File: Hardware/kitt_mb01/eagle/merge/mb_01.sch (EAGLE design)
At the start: 96 parts, among them CON1 ARDUINO_UNO, IC1.01 RT8293A, IC2.00 BQ24266RGET, IC3.01 LSM9DS1, P2 S2B-PH-K-S(LF)(SN), U6.01 TPS61032RSARPSDO-G16

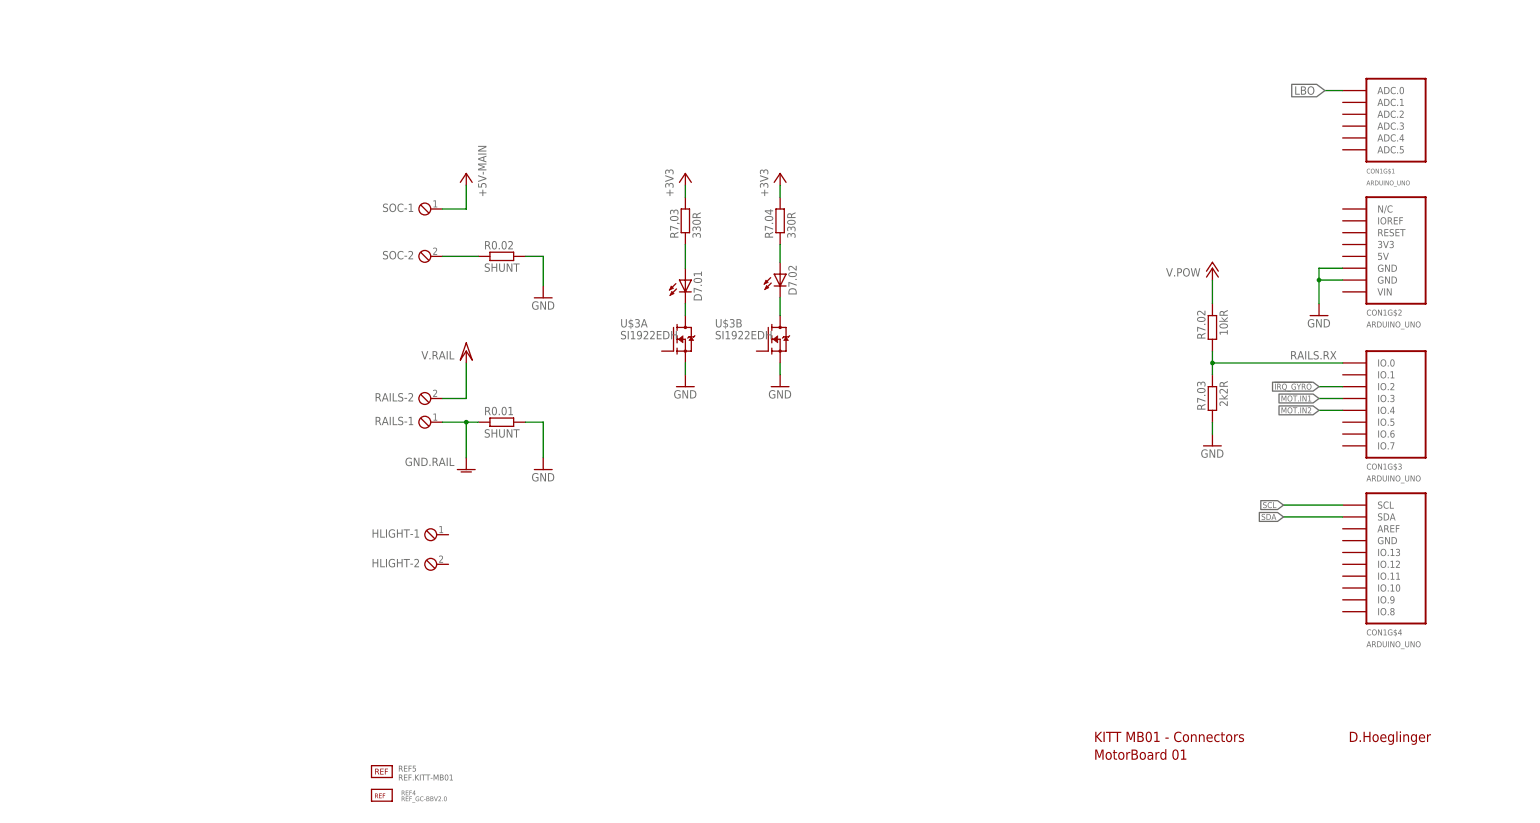
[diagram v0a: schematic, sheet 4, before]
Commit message: snapshot of board merge
a point about the flipped LEDs with a hole:
it's mounted in reverse with a hole as a makeshift lightguard,
...because maybe.
There are actual LEDs with an lens attached (see knightbright),
but regular ones work as well obviously.
Also it allows for text to be silk'd right next to it, which is sweet.
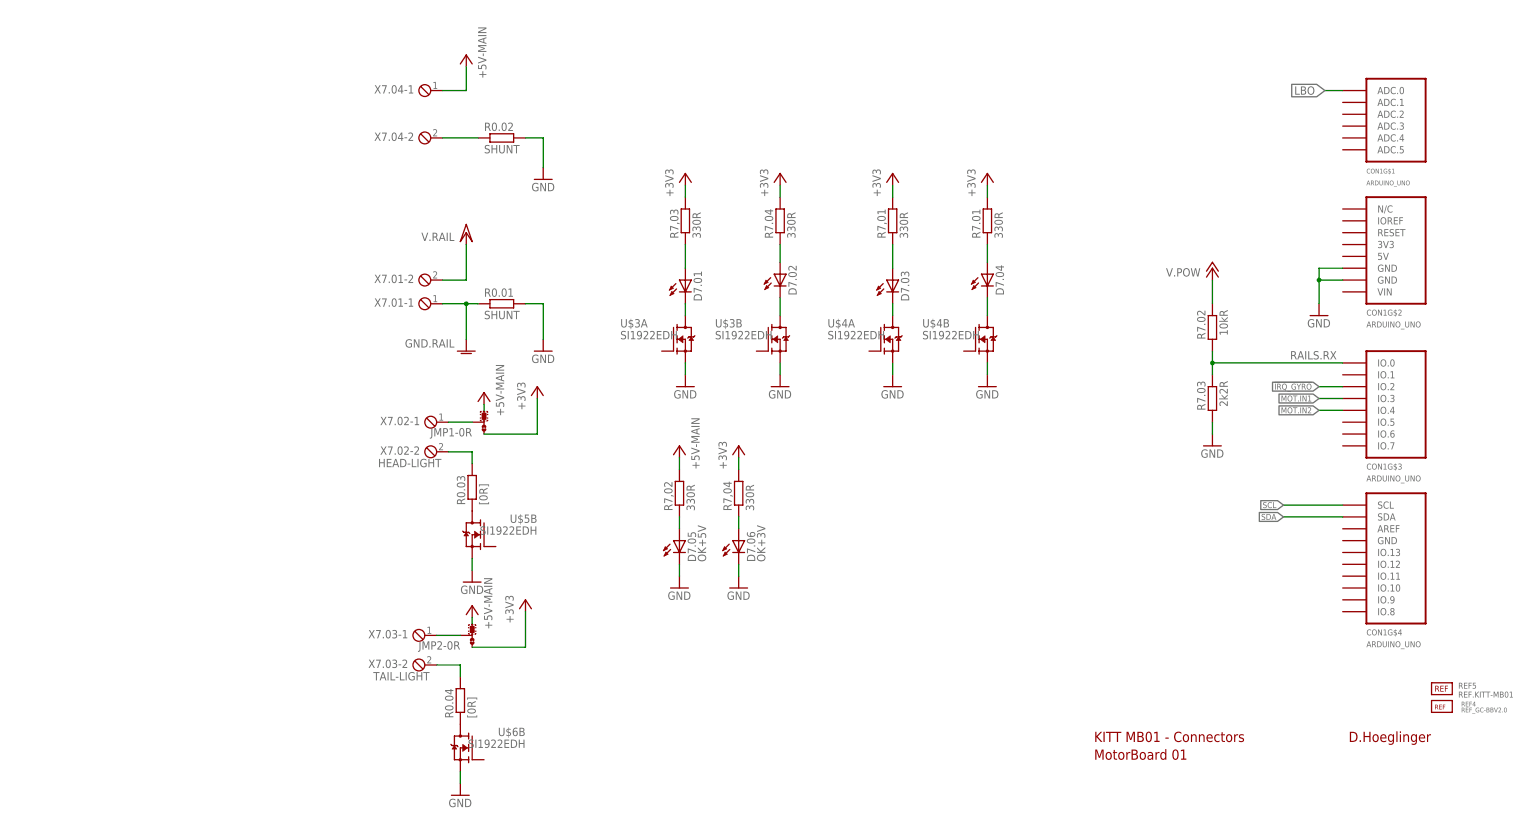
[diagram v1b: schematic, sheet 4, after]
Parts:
- removed HLIGHT, RAILS, SOC: (no value), con-phoenix-254:MPT2
- added D7.03, D7.04: (no value), led:LEDCHIPLED_0805
- added D7.05: OK+5V, led:LEDCHIPLED_1206
- added D7.06: OK+3V, led:LEDCHIPLED_1206
- added JMP1, JMP2: 0R-JUMPA, jump-0r-smd:0R-JUMPA
- added R0.03, R0.04: [0R], rcl:R-EU_R1206
- added R7,01, R7,02, R7,04, R7.01: 330R, rcl:R-EU_R0603
- added U$4, U$5, U$6: SI1922EDH, kitt.ic:SI1922EDH
- added X7.01, X7.04: (no value), con-phoenix-254:MPT2
- added X7.02: HEAD-LIGHT, con-phoenix-254:MPT2
- added X7.03: TAIL-LIGHT, con-phoenix-254:MPT2
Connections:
- new net N$28: D7.03.C, U$4A.D
- new net N$29: D7.03.A, R7,01.1
- new net N$30: D7.04.A, R7.01.1
- new net N$31: D7.04.C, U$4B.D
- new net N$32: D7.05.A, R7,02.1
- new net N$38: D7.06.A, R7,04.1
- new net N$42: R0.03.2, X7.02-2.1
- new net N$44: R0.03.1, U$5B.D
- new net N$45: JMP1-0R.2, X7.02-1.1
- new net N$46: R0.04.2, X7.03-2.1
- new net N$47: R0.04.1, U$6B.D
- new net N$48: JMP2-0R.2, X7.03-1.1
- net +3V3: now also JMP1-0R.1, JMP2-0R.1, R7,01.2, R7,04.2, R7.01.2
- net +5V: now also JMP1-0R.3, JMP2-0R.3, R7,02.2, X7.04-1.1; no longer SOC-1.1
- net GND: now also D7.05.C, D7.06.C, U$4A.S, U$4B.S, U$5B.S, U$6B.S
- net GNDA: now also X7.01-1.1; no longer RAILS-1.1
- net N$25: now also X7.04-2.1; no longer SOC-2.1
- net VCC/2: now also X7.01-2.1; no longer RAILS-2.1
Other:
- moved on the sheet: R0.01, R0.02, REF4, REF5

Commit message: snapshot of board merge - added possible port expander via i2c - did some more routing - connected battery indicator leds
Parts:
- added U1: MCP23017-E, kitt.ic:MCP23017-E
- D7.01, D7.02, D7.03, D7.04: device led:LEDCHIPLED_0805 -> led:LEDCHIPLED_1206
- X7.05: value (none) -> MOTOR
- renumbered SOC1 to X7.05
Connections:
- net IC2.0.!CHG: now also U$4A.G
- net IC2.0.!PG: now also U$4B.G
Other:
- note added: "TODO: INTERNAL PULLUP OR WHAT?"
- note added: "TODO: PORT EXPANDER? Pro: +Utility +Knight Rider Effects Con: -More $€ -More routes"

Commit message: snapshot of board merge  - it's going somewhere edition -
-> connected and routed head lights
-> did some power routing
-> next up: tail light
-> next² up: need for speedboards
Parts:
- removed U$5: SI1922EDH, kitt.ic:SI1922EDH
- added U7.01: SI1922EDH, kitt.ic:SI1922EDH
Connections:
- removed net N$44: R0.03.1, U$5B.D
- new net CAR.BLIGHT: CON1G$3.IO.5
- new net CAR.FLIGHT: CON1G$3.IO.6, U7.01A.G
- new net CAR.LAPCNT: CON1G$3.IO.7
- new net N$2: R0.03.1, U7.01A.D
- net GND: now also U7.01A.S; no longer U$5B.S
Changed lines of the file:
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@@
 <part name="+3V11" library="supply1" deviceset="+3V3" device=""/>
 <part name="P+5VMAIN4" library="supply1" deviceset="+5V" device="" value="+5V-MAIN"/>
-<part name="U$5" library="kitt.ic" deviceset="SI1922EDH" device=""/>
+<part name="U7.01" library="kitt.ic" deviceset="SI1922EDH" device=""/>
 <part name="R0.03" library="rcl" deviceset="R-EU_" device="R1206" value="[0R]"/>
 <part name="GND33" library="supply1" deviceset="GND" device=""/>
@@
 <instance part="+3V11" gate="G$1" x="86.36" y="83.82"/>
 <instance part="P+5VMAIN4" gate="1" x="73.66" y="83.82" rot="MR0"/>
-<instance part="U$5" gate="B" x="31.75" y="78.74" rot="MR0"/>
 <instance part="R0.03" gate="G$1" x="29.21" y="88.9" rot="R90"/>
 <instance part="GND33" gate="1" x="29.21" y="68.58"/>
@@
 <instance part="P+5VMAIN6" gate="1" x="29.21" y="63.5" rot="MR0"/>
 <instance part="+3V12" gate="G$1" x="40.64" y="64.77"/>
+<instance part="U7.01" gate="A" x="31.75" y="78.74" rot="MR0"/>
 </instances>
 <busses>
@@
 <segment>
 <pinref part="GND33" gate="1" pin="GND"/>
-<pinref part="U$5" gate="B" pin="S"/>
 <wire x1="29.21" y1="71.12" x2="29.21" y2="73.66" width="0.1524" layer="91"/>
+<pinref part="U7.01" gate="A" pin="S"/>
 </segment>
 <segment>
@@
 </segment>
 </net>
-<net name="N$44" class="0">
-<segment>
-<pinref part="U$5" gate="B" pin="D"/>
-<pinref part="R0.03" gate="G$1" pin="1"/>
-</segment>
-</net>
 <net name="N$45" class="0">
 <segment>
@@
 </segment>
 </net>
+<net name="N$2" class="0">
+<segment>
+<pinref part="R0.03" gate="G$1" pin="1"/>
+<pinref part="U7.01" gate="A" pin="D"/>
+</segment>
+</net>
+<net name="CAR.FLIGHT" class="0">
+<segment>
+<pinref part="U7.01" gate="A" pin="G"/>
+<wire x1="34.29" y1="76.2" x2="43.18" y2="76.2" width="0.1524" layer="91"/>
+<label x="43.18" y="76.2" size="1.778" layer="95" xref="yes"/>
+</segment>
+<segment>
+<label x="210.82" y="86.36" size="1.27" layer="95" rot="R180" xref="yes"/>
+<pinref part="CON1" gate="G$3" pin="IO.6"/>
+<wire x1="210.82" y1="86.36" x2="215.9" y2="86.36" width="0.1524" layer="91"/>
+</segment>
+</net>
+<net name="CAR.BLIGHT" class="0">
+<segment>
+<label x="210.82" y="88.9" size="1.27" layer="95" rot="R180" xref="yes"/>
+<wire x1="210.82" y1="88.9" x2="215.9" y2="88.9" width="0.1524" layer="91"/>
+<pinref part="CON1" gate="G$3" pin="IO.5"/>
+</segment>
+</net>
+<net name="CAR.LAPCNT" class="0">
+<segment>
+<pinref part="CON1" gate="G$3" pin="IO.7"/>
+<wire x1="215.9" y1="83.82" x2="210.82" y2="83.82" width="0.1524" layer="91"/>
+<label x="210.82" y="83.82" size="1.27" layer="95" rot="R180" xref="yes"/>
+</segment>
+</net>

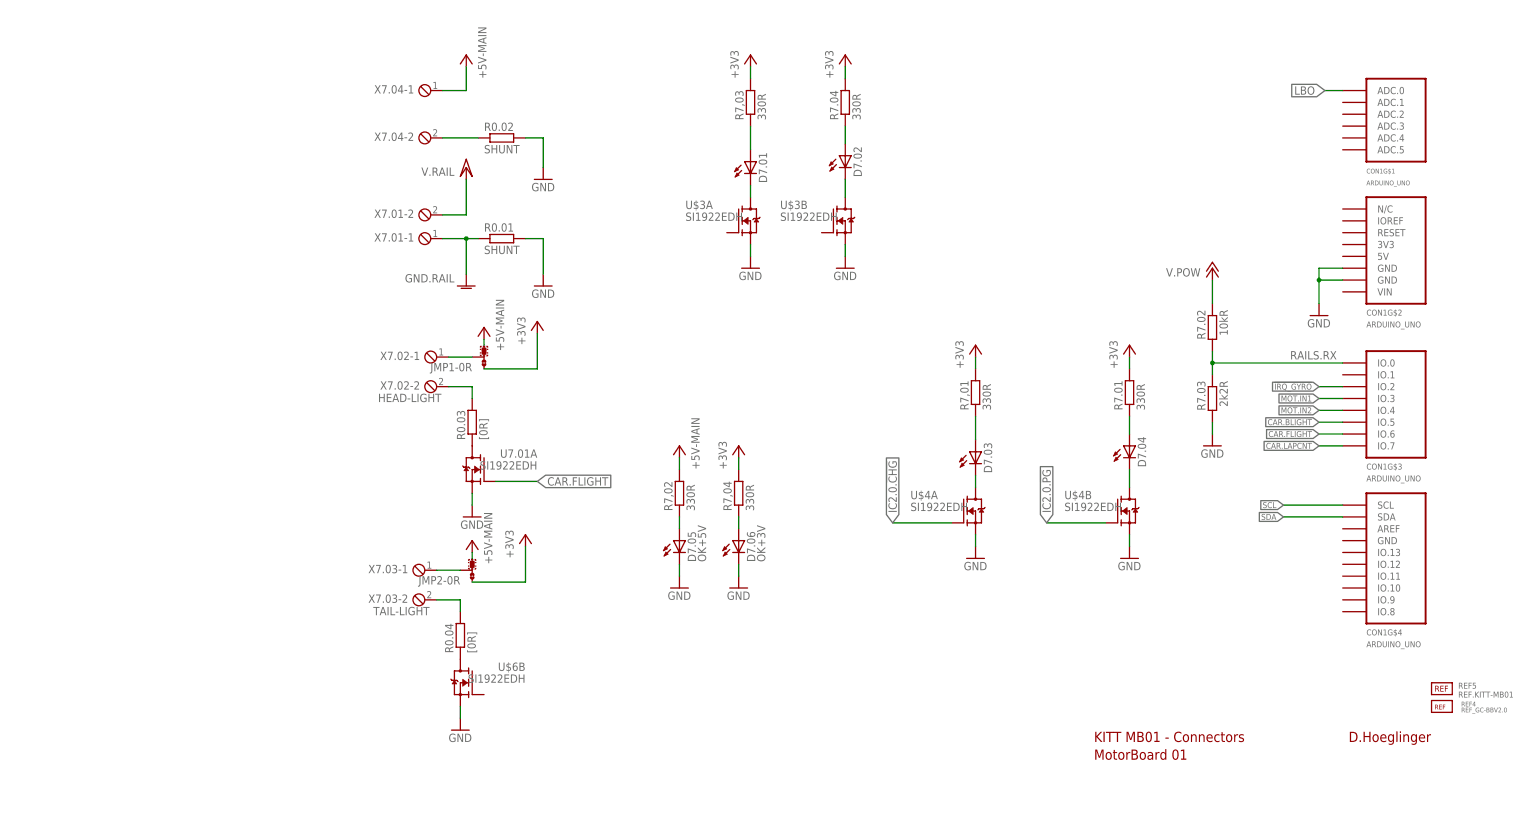
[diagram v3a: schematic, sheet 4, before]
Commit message: snapshot of board merge : nearing it's "completion" edition
things to do:
-> either find a good placement for GP-indicators,
   or drop alltogether (what purpose?)
-> (re)move idea about port expander (DB01 maybe?)
-> add some fancy-pants logos, fiducial marks and layer count
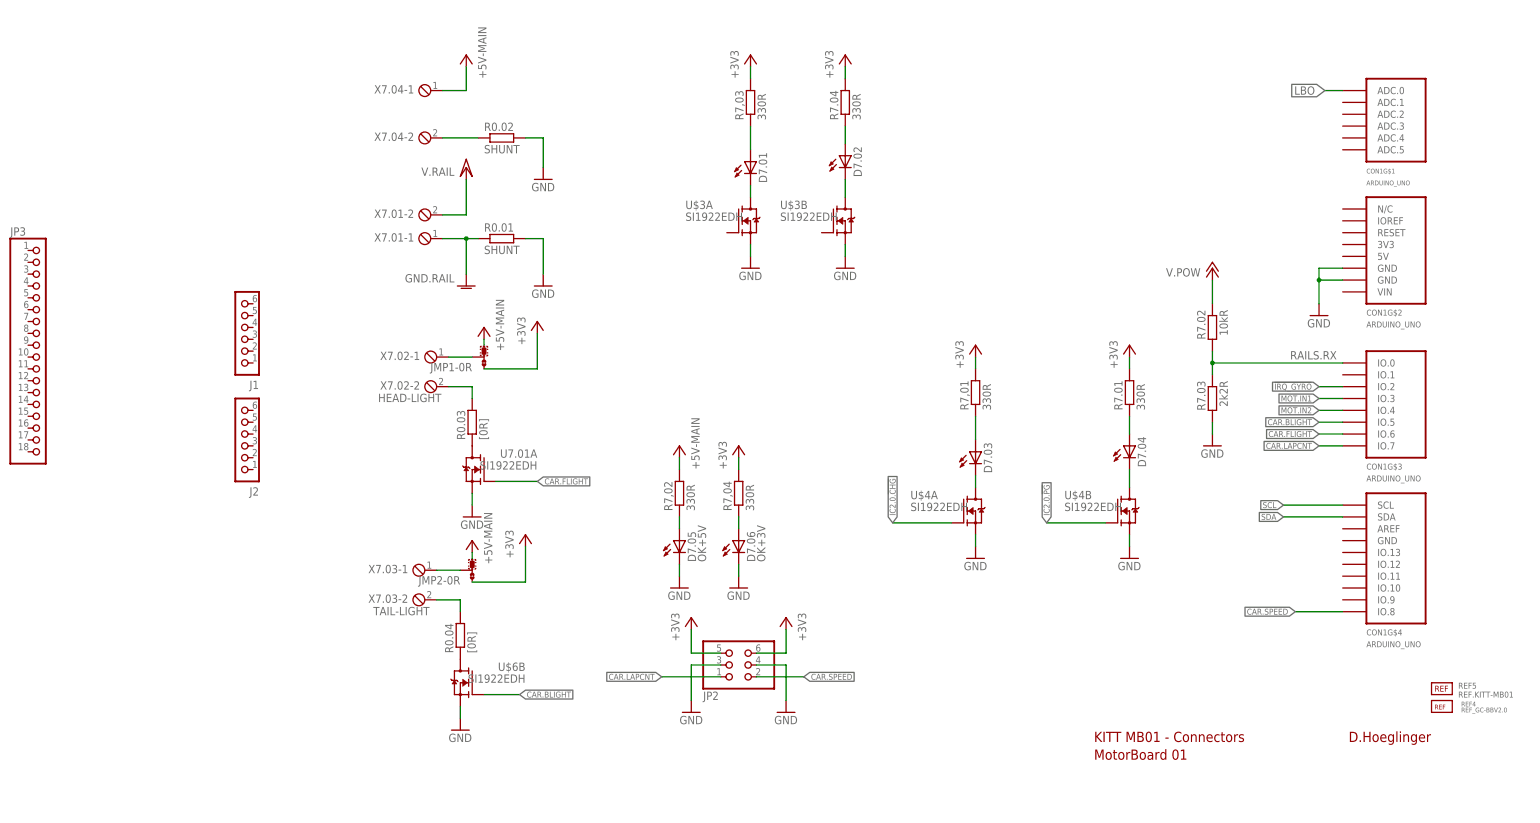
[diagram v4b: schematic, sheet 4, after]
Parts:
- added J1, J2: CON_HEADER_1X06-SMD-RIGHT-ANGLED, dp_devices:CON_HEADER_1X06-SMD-RIGHT-ANGLED
- added JP2: (no value), pinhead:PINHD-2X3/90
- added JP3: (no value), pinhead:PINHD-1X18/90
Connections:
- new net CAR.SPEED: CON1G$4.IO.8, JP2.2
- net +3V3: now also JP2.5, JP2.6
- net CAR.BLIGHT: now also U$6B.G
- net CAR.LAPCNT: now also JP2.1
- net GND: now also JP2.3, JP2.4
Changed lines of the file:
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@@
 <part name="FRAME7" library="frames" deviceset="A4L-LOC" device=""/>
 <part name="U1" library="kitt.ic" deviceset="MCP23017-E" device=""/>
+<part name="JP2" library="pinhead" deviceset="PINHD-2X3" device="/90"/>
+<part name="GND35" library="supply1" deviceset="GND" device=""/>
+<part name="+3V13" library="supply1" deviceset="+3V3" device=""/>
+<part name="+3V14" library="supply1" deviceset="+3V3" device=""/>
+<part name="GND36" library="supply1" deviceset="GND" device=""/>
+<part name="JP3" library="pinhead" deviceset="PINHD-1X18" device="/90"/>
+<part name="J1" library="dp_devices" deviceset="CON_HEADER_1X06" device="-SMD-RIGHT-ANGLED"/>
+<part name="J2" library="dp_devices" deviceset="CON_HEADER_1X06" device="-SMD-RIGHT-ANGLED"/>
 </parts>
 <sheets>
@@
 <instance part="+3V12" gate="G$1" x="40.64" y="64.77"/>
 <instance part="U7.01" gate="A" x="31.75" y="78.74" rot="MR0"/>
+<instance part="JP2" gate="A" x="85.09" y="36.83" rot="MR180"/>
+<instance part="GND35" gate="1" x="76.2" y="26.67"/>
+<instance part="+3V13" gate="G$1" x="76.2" y="46.99"/>
+<instance part="+3V14" gate="G$1" x="96.52" y="46.99" rot="MR0"/>
+<instance part="GND36" gate="1" x="96.52" y="26.67"/>
+<instance part="JP3" gate="A" x="-63.5" y="105.41"/>
+<instance part="J1" gate="J" x="-17.78" y="106.68" rot="R180"/>
+<instance part="J2" gate="J" x="-17.78" y="83.82" rot="R180"/>
 </instances>
 <busses>
@@
 <wire x1="26.67" y1="25.4" x2="26.67" y2="27.94" width="0.1524" layer="91"/>
 </segment>
+<segment>
+<pinref part="GND35" gate="1" pin="GND"/>
+<pinref part="JP2" gate="A" pin="3"/>
+<wire x1="76.2" y1="29.21" x2="76.2" y2="36.83" width="0.1524" layer="91"/>
+<wire x1="76.2" y1="36.83" x2="82.55" y2="36.83" width="0.1524" layer="91"/>
+</segment>
+<segment>
+<pinref part="GND36" gate="1" pin="GND"/>
+<pinref part="JP2" gate="A" pin="4"/>
+<wire x1="96.52" y1="29.21" x2="96.52" y2="36.83" width="0.1524" layer="91"/>
+<wire x1="96.52" y1="36.83" x2="90.17" y2="36.83" width="0.1524" layer="91"/>
+</segment>
 </net>
 <net name="RAILS.RX" class="0">
@@
 <wire x1="40.64" y1="54.61" x2="40.64" y2="62.23" width="0.1524" layer="91"/>
 </segment>
+<segment>
+<pinref part="+3V13" gate="G$1" pin="+3V3"/>
+<pinref part="JP2" gate="A" pin="5"/>
+<wire x1="76.2" y1="44.45" x2="76.2" y2="39.37" width="0.1524" layer="91"/>
+<wire x1="76.2" y1="39.37" x2="82.55" y2="39.37" width="0.1524" layer="91"/>
+</segment>
+<segment>
+<pinref part="JP2" gate="A" pin="6"/>
+<pinref part="+3V14" gate="G$1" pin="+3V3"/>
+<wire x1="90.17" y1="39.37" x2="96.52" y2="39.37" width="0.1524" layer="91"/>
+<wire x1="96.52" y1="39.37" x2="96.52" y2="44.45" width="0.1524" layer="91"/>
+</segment>
 </net>
 <net name="N$25" class="0">
@@
 <net name="IC2.0.!CHG" class="0">
 <segment>
-<label x="119.38" y="67.31" size="1.778" layer="95" rot="R90" xref="yes"/>
+<label x="119.38" y="67.31" size="1.27" layer="95" rot="R90" xref="yes"/>
 <pinref part="U$4" gate="A" pin="G"/>
 <wire x1="119.38" y1="67.31" x2="132.08" y2="67.31" width="0.1524" layer="91"/>
@@
 <segment>
 <wire x1="152.4" y1="67.31" x2="165.1" y2="67.31" width="0.1524" layer="91"/>
-<label x="152.4" y="67.31" size="1.778" layer="95" rot="R90" xref="yes"/>
+<label x="152.4" y="67.31" size="1.27" layer="95" rot="R90" xref="yes"/>
 <pinref part="U$4" gate="B" pin="G"/>
 </segment>
@@
 <pinref part="U7.01" gate="A" pin="G"/>
 <wire x1="34.29" y1="76.2" x2="43.18" y2="76.2" width="0.1524" layer="91"/>
-<label x="43.18" y="76.2" size="1.778" layer="95" xref="yes"/>
+<label x="43.18" y="76.2" size="1.27" layer="95" xref="yes"/>
 </segment>
 <segment>
@@
 <pinref part="CON1" gate="G$3" pin="IO.5"/>
 </segment>
+<segment>
+<wire x1="31.75" y1="30.48" x2="39.37" y2="30.48" width="0.1524" layer="91"/>
+<pinref part="U$6" gate="B" pin="G"/>
+<label x="39.37" y="30.48" size="1.27" layer="95" xref="yes"/>
+</segment>
 </net>
 <net name="CAR.LAPCNT" class="0">
@@
 <label x="210.82" y="83.82" size="1.27" layer="95" rot="R180" xref="yes"/>
 </segment>
-</net>
+<segment>
+<wire x1="69.85" y1="34.29" x2="82.55" y2="34.29" width="0.1524" layer="91"/>
+<label x="69.85" y="34.29" size="1.27" layer="95" rot="R180" xref="yes"/>
+<pinref part="JP2" gate="A" pin="1"/>
+</segment>
+</net>
+<net name="CAR.SPEED" class="0">
+<segment>
+<pinref part="CON1" gate="G$4" pin="IO.8"/>
+<wire x1="215.9" y1="48.26" x2="205.74" y2="48.26" width="0.1524" layer="91"/>
+<label x="205.74" y="48.26" size="1.27" layer="95" rot="R180" xref="yes"/>
+</segment>
+<segment>
+<label x="100.33" y="34.29" size="1.27" layer="95" xref="yes"/>
+<wire x1="90.17" y1="34.29" x2="100.33" y2="34.29" width="0.1524" layer="91"/>
+<pinref part="JP2" gate="A" pin="2"/>
+</segment>
+</net>
